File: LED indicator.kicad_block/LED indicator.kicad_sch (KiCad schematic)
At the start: 2 parts

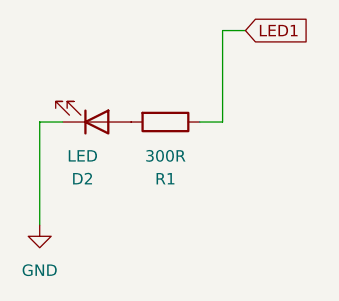
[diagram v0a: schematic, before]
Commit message: changed resistor value from "300R" to just 300
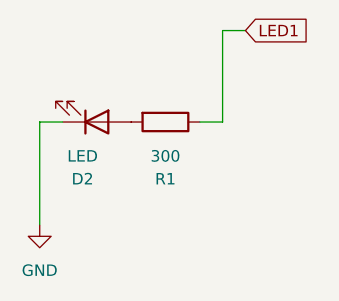
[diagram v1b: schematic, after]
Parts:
- R1: value 300R -> 300
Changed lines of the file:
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@@
 			)
 		)
-		(property "Value" "300R"
+		(property "Value" "300"
 			(at 232.41 96.52 90)
 			(show_name no)
